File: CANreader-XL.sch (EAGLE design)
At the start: 100 parts, among them IC1 STM32F107RBT, IC2 TJA1055T/3, IC3 BD9G101G, IC4 LM1117IMPX-3.3, IC5 MCP2562-SOIC8, IC7 DP83848I, Q1 25MHz, SW1 SLEEP, SW2 TERM, U1 HC_05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

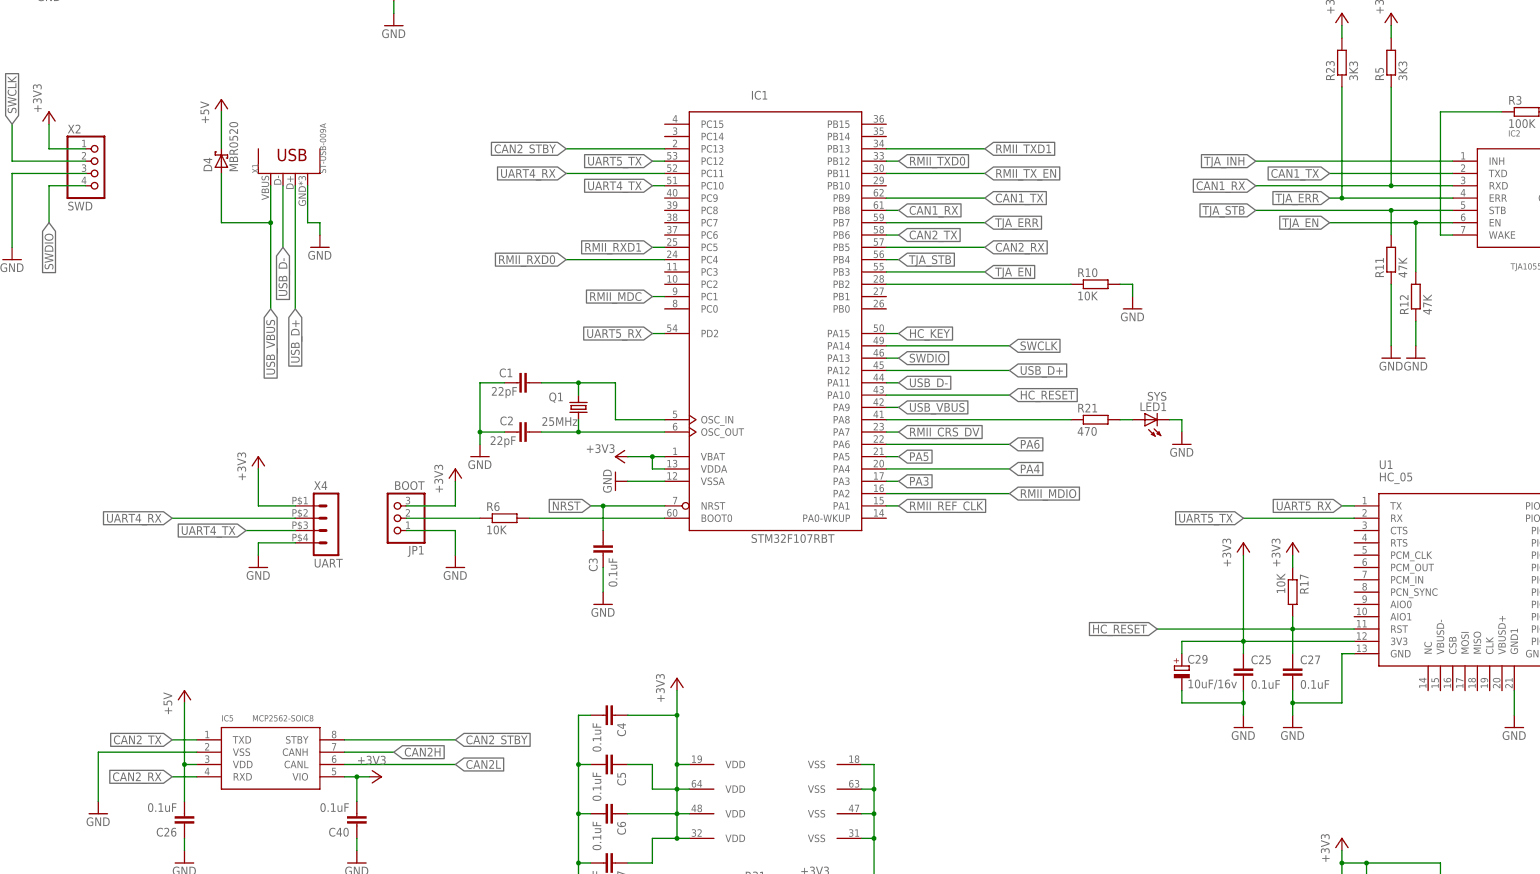
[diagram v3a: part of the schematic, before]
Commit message: Swap UART, CAN for better routing
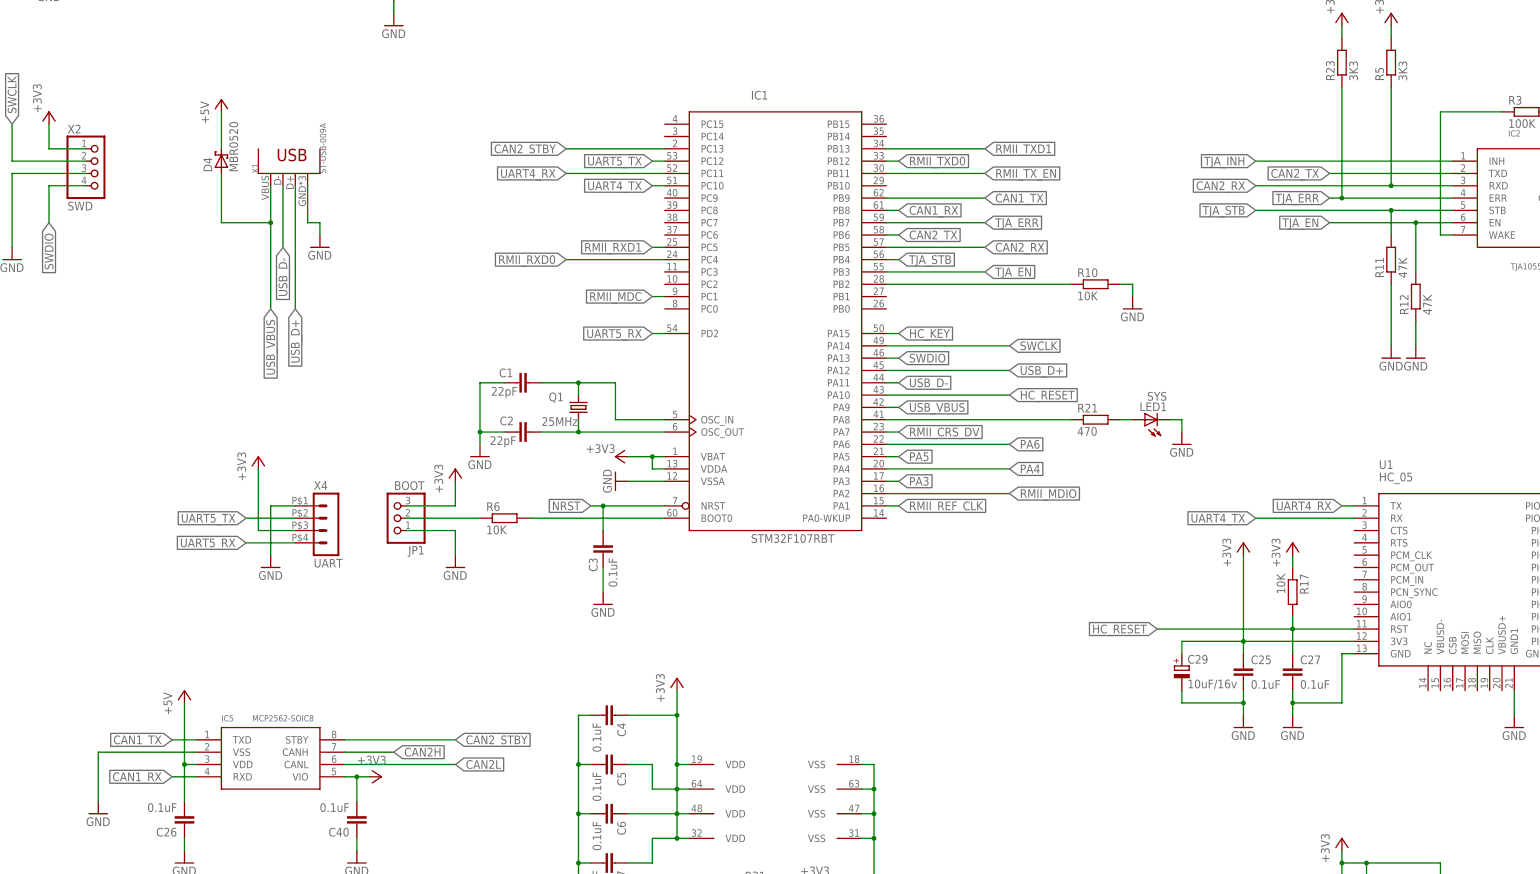
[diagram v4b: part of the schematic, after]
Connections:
- net +3V3: now also X4.3; no longer X4.1
- net CAN1_RX: now also IC5.RXD; no longer IC2.RXD, R5.1
- net CAN1_TX: now also IC5.TXD; no longer IC2.TXD
- net CAN2_RX: now also IC2.RXD, R5.1; no longer IC5.RXD
- net CAN2_TX: now also IC2.TXD; no longer IC5.TXD
- net GND: now also X4.1; no longer X4.4
- net UART4_RX: now also U1.TX; no longer X4.2
- net UART4_TX: now also U1.RX; no longer X4.3
- net UART5_RX: now also X4.4; no longer U1.TX
- net UART5_TX: now also X4.2; no longer U1.RX
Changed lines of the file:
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@@
 <?xml version="1.0" encoding="utf-8"?>
 <!DOCTYPE eagle SYSTEM "eagle.dtd">
-<eagle version="7.5.0">
+<eagle version="7.6.0">
 <drawing>
 <settings>
@@
 <instance part="R10" gate="G$1" x="139.7" y="45.72"/>
 <instance part="GND16" gate="1" x="7.62" y="-12.7"/>
-<instance part="GND17" gate="1" x="-33.02" y="-12.7"/>
+<instance part="GND17" gate="1" x="-30.48" y="-12.7"/>
 <instance part="D4" gate="D$1" x="-40.64" y="71.12" rot="R90"/>
 <instance part="GND18" gate="1" x="180.34" y="162.56" rot="R270"/>
@@
 <segment>
 <pinref part="GND17" gate="1" pin="GND"/>
-<wire x1="-25.4" y1="-7.62" x2="-33.02" y2="-7.62" width="0.1524" layer="91"/>
-<wire x1="-33.02" y1="-7.62" x2="-33.02" y2="-10.16" width="0.1524" layer="91"/>
-<pinref part="X4" gate="G$1" pin="4"/>
+<wire x1="-30.48" y1="-10.16" x2="-30.48" y2="0" width="0.1524" layer="91"/>
+<pinref part="X4" gate="G$1" pin="1"/>
+<wire x1="-30.48" y1="0" x2="-25.4" y2="0" width="0.1524" layer="91"/>
 </segment>
 <segment>
@@
 <segment>
 <pinref part="+3V9" gate="G$1" pin="+3V3"/>
-<wire x1="-25.4" y1="0" x2="-33.02" y2="0" width="0.1524" layer="91"/>
-<wire x1="-33.02" y1="0" x2="-33.02" y2="7.62" width="0.1524" layer="91"/>
-<pinref part="X4" gate="G$1" pin="1"/>
+<wire x1="-33.02" y1="-5.08" x2="-33.02" y2="7.62" width="0.1524" layer="91"/>
+<pinref part="X4" gate="G$1" pin="3"/>
+<wire x1="-33.02" y1="-5.08" x2="-25.4" y2="-5.08" width="0.1524" layer="91"/>
 </segment>
 <segment>
@@
 <net name="CAN1_RX" class="0">
 <segment>
-<pinref part="IC2" gate="G$1" pin="RXD"/>
-<pinref part="R5" gate="G$1" pin="1"/>
-<wire x1="200.66" y1="66.04" x2="213.36" y2="66.04" width="0.1524" layer="91"/>
-<wire x1="200.66" y1="86.36" x2="200.66" y2="66.04" width="0.1524" layer="91"/>
-<junction x="200.66" y="66.04"/>
-<wire x1="200.66" y1="66.04" x2="172.72" y2="66.04" width="0.1524" layer="91"/>
-<label x="172.72" y="66.04" size="1.778" layer="95" rot="R180" xref="yes"/>
-</segment>
-<segment>
 <label x="99.06" y="60.96" size="1.778" layer="95" xref="yes"/>
 <pinref part="IC1" gate="MCU" pin="PB8"/>
 <wire x1="99.06" y1="60.96" x2="96.52" y2="60.96" width="0.1524" layer="91"/>
+</segment>
+<segment>
+<pinref part="IC5" gate="G$1" pin="RXD"/>
+<wire x1="-45.72" y1="-55.88" x2="-50.8" y2="-55.88" width="0.1524" layer="91"/>
+<label x="-50.8" y="-55.88" size="1.778" layer="95" rot="R180" xref="yes"/>
 </segment>
 </net>
@@
 </segment>
 <segment>
-<label x="-50.8" y="-2.54" size="1.778" layer="95" rot="R180" xref="yes"/>
-<wire x1="-25.4" y1="-2.54" x2="-50.8" y2="-2.54" width="0.1524" layer="91"/>
-<pinref part="X4" gate="G$1" pin="2"/>
+<pinref part="U1" gate="G$1" pin="TX"/>
+<wire x1="193.04" y1="0" x2="190.5" y2="0" width="0.1524" layer="91"/>
+<label x="190.5" y="0" size="1.778" layer="95" rot="R180" xref="yes"/>
 </segment>
 </net>
@@
 </segment>
 <segment>
-<label x="-35.56" y="-5.08" size="1.778" layer="95" rot="R180" xref="yes"/>
-<wire x1="-35.56" y1="-5.08" x2="-25.4" y2="-5.08" width="0.1524" layer="91"/>
-<pinref part="X4" gate="G$1" pin="3"/>
+<pinref part="U1" gate="G$1" pin="RX"/>
+<wire x1="193.04" y1="-2.54" x2="172.72" y2="-2.54" width="0.1524" layer="91"/>
+<label x="172.72" y="-2.54" size="1.778" layer="95" rot="R180" xref="yes"/>
 </segment>
 </net>
@@
 </segment>
 <segment>
-<pinref part="U1" gate="G$1" pin="RX"/>
-<wire x1="193.04" y1="-2.54" x2="170.18" y2="-2.54" width="0.1524" layer="91"/>
-<label x="170.18" y="-2.54" size="1.778" layer="95" rot="R180" xref="yes"/>
+<pinref part="X4" gate="G$1" pin="2"/>
+<wire x1="-25.4" y1="-2.54" x2="-35.56" y2="-2.54" width="0.1524" layer="91"/>
+<label x="-35.56" y="-2.54" size="1.778" layer="95" rot="R180" xref="yes"/>
 </segment>
 </net>
@@
 </segment>
 <segment>
-<pinref part="U1" gate="G$1" pin="TX"/>
-<wire x1="193.04" y1="0" x2="190.5" y2="0" width="0.1524" layer="91"/>
-<label x="190.5" y="0" size="1.778" layer="95" rot="R180" xref="yes"/>
+<pinref part="X4" gate="G$1" pin="4"/>
+<wire x1="-25.4" y1="-7.62" x2="-35.56" y2="-7.62" width="0.1524" layer="91"/>
+<label x="-35.56" y="-7.62" size="1.778" layer="95" rot="R180" xref="yes"/>
 </segment>
 </net>
@@
 <net name="CAN1_TX" class="0">
 <segment>
-<pinref part="IC2" gate="G$1" pin="TXD"/>
-<wire x1="213.36" y1="68.58" x2="187.96" y2="68.58" width="0.1524" layer="91"/>
-<label x="187.96" y="68.58" size="1.778" layer="95" rot="R180" xref="yes"/>
-</segment>
-<segment>
 <label x="116.84" y="63.5" size="1.778" layer="95" xref="yes"/>
 <wire x1="96.52" y1="63.5" x2="116.84" y2="63.5" width="0.1524" layer="91"/>
 <pinref part="IC1" gate="MCU" pin="PB9"/>
+</segment>
+<segment>
+<pinref part="IC5" gate="G$1" pin="TXD"/>
+<wire x1="-45.72" y1="-48.26" x2="-50.8" y2="-48.26" width="0.1524" layer="91"/>
+<label x="-50.8" y="-48.26" size="1.778" layer="95" rot="R180" xref="yes"/>
 </segment>
 </net>
@@
 <net name="CAN2_TX" class="0">
 <segment>
-<wire x1="-45.72" y1="-48.26" x2="-50.8" y2="-48.26" width="0.1524" layer="91"/>
-<label x="-50.8" y="-48.26" size="1.778" layer="95" rot="R180" xref="yes"/>
-<pinref part="IC5" gate="G$1" pin="TXD"/>
-</segment>
-<segment>
 <label x="99.06" y="55.88" size="1.778" layer="95" xref="yes"/>
 <pinref part="IC1" gate="MCU" pin="PB6"/>
 <wire x1="99.06" y1="55.88" x2="96.52" y2="55.88" width="0.1524" layer="91"/>
 </segment>
+<segment>
+<pinref part="IC2" gate="G$1" pin="TXD"/>
+<wire x1="213.36" y1="68.58" x2="187.96" y2="68.58" width="0.1524" layer="91"/>
+<label x="187.96" y="68.58" size="1.778" layer="95" rot="R180" xref="yes"/>
+</segment>
 </net>
 <net name="CAN2_RX" class="0">
-<segment>
-<wire x1="-45.72" y1="-55.88" x2="-50.8" y2="-55.88" width="0.1524" layer="91"/>
-<label x="-50.8" y="-55.88" size="1.778" layer="95" rot="R180" xref="yes"/>
-<pinref part="IC5" gate="G$1" pin="RXD"/>
-</segment>
 <segment>
 <label x="116.84" y="53.34" size="1.778" layer="95" xref="yes"/>
@@
 <wire x1="116.84" y1="53.34" x2="96.52" y2="53.34" width="0.1524" layer="91"/>
 </segment>
-</net>
+<segment>
+<pinref part="IC2" gate="G$1" pin="RXD"/>
+<pinref part="R5" gate="G$1" pin="1"/>
+<wire x1="213.36" y1="66.04" x2="200.66" y2="66.04" width="0.1524" layer="91"/>
+<wire x1="200.66" y1="66.04" x2="200.66" y2="86.36" width="0.1524" layer="91"/>
+<wire x1="200.66" y1="66.04" x2="172.72" y2="66.04" width="0.1524" layer="91"/>
+<junction x="200.66" y="66.04"/>
+<label x="172.72" y="66.04" size="1.778" layer="95" rot="R180" xref="yes"/>
+</segment>
+</net>

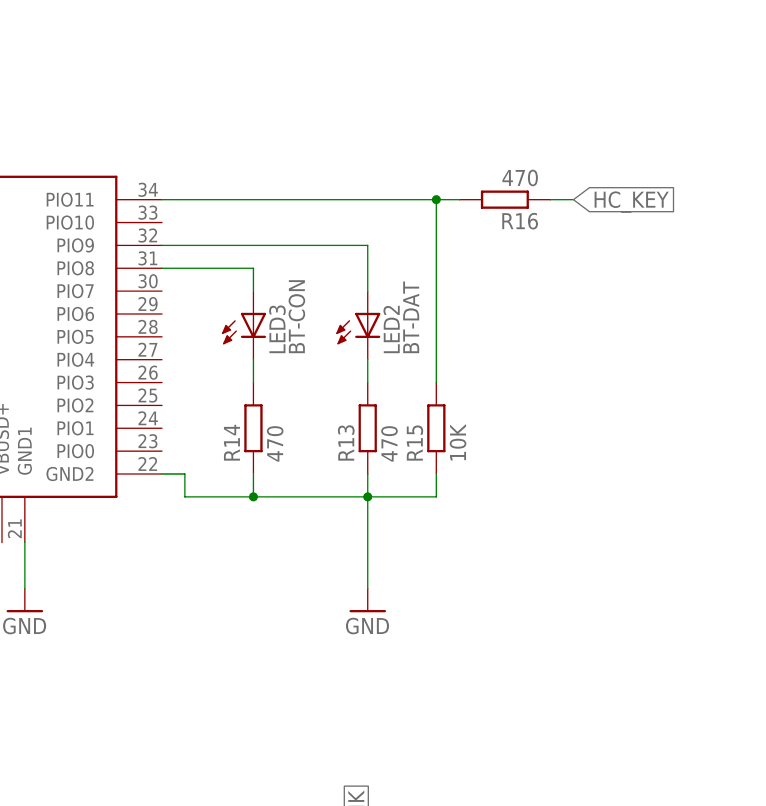
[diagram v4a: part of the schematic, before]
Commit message: Swap ports
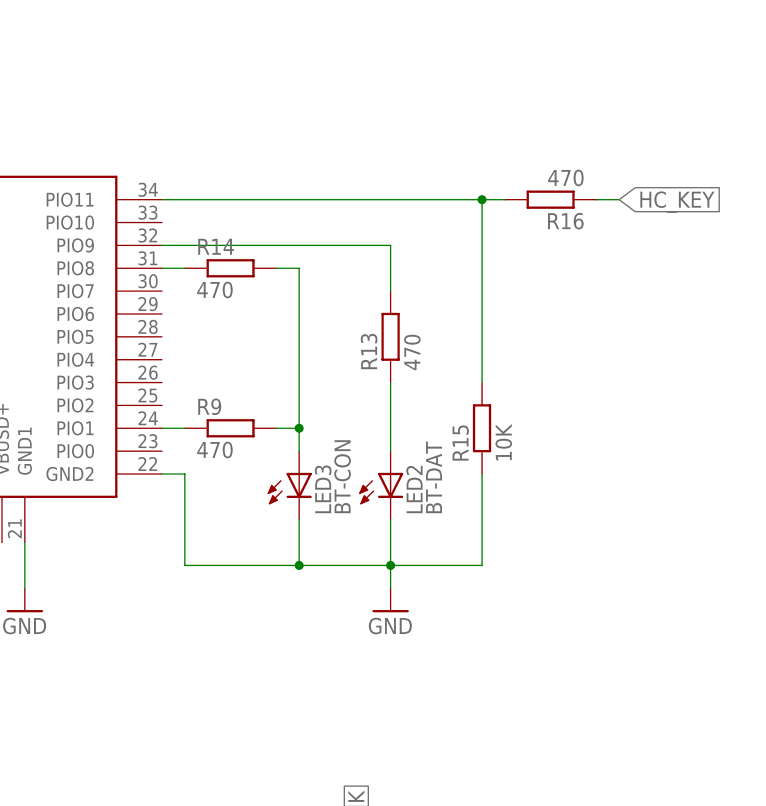
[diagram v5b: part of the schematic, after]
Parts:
- added R9: 470, rcl:R-EU_R0805
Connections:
- new net N$33: LED3.A, R14.2, R9.2
- net GND: now also LED2.C, LED3.C; no longer R13.1, R14.1
- net N$10: now also R13.2; no longer LED2.A
- net N$11: now also LED2.A, R13.1; no longer LED2.C, R13.2
- net N$13: now also R9.1, U1.PIO1; no longer LED3.C, R14.2
- net N$5: now also R14.1; no longer LED3.A
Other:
- moved on the sheet: LED2, LED3, R13, R14, R15, R16
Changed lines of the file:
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@@
 <part name="+3V7" library="supply1" deviceset="+3V3" device=""/>
 <part name="R6" library="rcl" deviceset="R-EU_" device="R0805" value="10K"/>
+<part name="R9" library="rcl" deviceset="R-EU_" device="R0805" value="470"/>
 </parts>
 <sheets>
@@
 <instance part="C25" gate="G$1" x="170.18" y="-33.02"/>
 <instance part="+3V5" gate="G$1" x="180.34" y="-7.62"/>
-<instance part="R13" gate="G$1" x="264.16" y="-25.4" rot="R90"/>
-<instance part="R14" gate="G$1" x="251.46" y="-25.4" rot="R90"/>
-<instance part="R15" gate="G$1" x="271.78" y="-25.4" rot="R90"/>
-<instance part="R16" gate="G$1" x="279.4" y="0" rot="R180"/>
+<instance part="R13" gate="G$1" x="266.7" y="-15.24" rot="R90"/>
+<instance part="R14" gate="G$1" x="248.92" y="-7.62"/>
+<instance part="R15" gate="G$1" x="276.86" y="-25.4" rot="R90"/>
+<instance part="R16" gate="G$1" x="284.48" y="0" rot="R180"/>
 <instance part="R17" gate="G$1" x="180.34" y="-17.78" rot="R270"/>
 <instance part="GND22" gate="1" x="12.7" y="10.16"/>
@@
 <instance part="GND31" gate="1" x="93.98" y="-83.82"/>
 <instance part="R22" gate="G$1" x="-43.18" y="-106.68" rot="R270"/>
-<instance part="LED2" gate="G$1" x="264.16" y="-12.7"/>
-<instance part="LED3" gate="G$1" x="251.46" y="-12.7"/>
+<instance part="LED2" gate="G$1" x="266.7" y="-30.48"/>
+<instance part="LED3" gate="G$1" x="256.54" y="-30.48"/>
 <instance part="LED1" gate="G$1" x="149.86" y="17.78" rot="R90"/>
 <instance part="SW2" gate="G$1" x="-55.88" y="-104.14"/>
@@
 <instance part="C27" gate="G$1" x="180.34" y="-33.02"/>
 <instance part="GND33" gate="1" x="180.34" y="-45.72"/>
-<instance part="GND34" gate="1" x="264.16" y="-45.72"/>
+<instance part="GND34" gate="1" x="266.7" y="-45.72"/>
 <instance part="GND35" gate="1" x="170.18" y="-45.72"/>
 <instance part="C11" gate="G$1" x="106.68" y="132.08"/>
@@
 <instance part="+3V7" gate="G$1" x="7.62" y="7.62"/>
 <instance part="R6" gate="G$1" x="17.78" y="-2.54"/>
+<instance part="R9" gate="G$1" x="248.92" y="-25.4"/>
 </instances>
 <busses>
@@
 <pinref part="U1" gate="G$1" pin="GND2"/>
 <wire x1="243.84" y1="-30.48" x2="241.3" y2="-30.48" width="0.1524" layer="91"/>
-<wire x1="243.84" y1="-33.02" x2="243.84" y2="-30.48" width="0.1524" layer="91"/>
+<wire x1="243.84" y1="-40.64" x2="243.84" y2="-30.48" width="0.1524" layer="91"/>
 <pinref part="R15" gate="G$1" pin="1"/>
-<wire x1="264.16" y1="-33.02" x2="251.46" y2="-33.02" width="0.1524" layer="91"/>
-<wire x1="251.46" y1="-33.02" x2="243.84" y2="-33.02" width="0.1524" layer="91"/>
-<wire x1="271.78" y1="-30.48" x2="271.78" y2="-33.02" width="0.1524" layer="91"/>
-<wire x1="271.78" y1="-33.02" x2="264.16" y2="-33.02" width="0.1524" layer="91"/>
-<pinref part="R13" gate="G$1" pin="1"/>
-<wire x1="264.16" y1="-30.48" x2="264.16" y2="-33.02" width="0.1524" layer="91"/>
-<junction x="264.16" y="-33.02"/>
-<pinref part="R14" gate="G$1" pin="1"/>
-<wire x1="251.46" y1="-30.48" x2="251.46" y2="-33.02" width="0.1524" layer="91"/>
-<junction x="251.46" y="-33.02"/>
+<wire x1="266.7" y1="-40.64" x2="256.54" y2="-40.64" width="0.1524" layer="91"/>
+<wire x1="256.54" y1="-40.64" x2="243.84" y2="-40.64" width="0.1524" layer="91"/>
+<wire x1="276.86" y1="-30.48" x2="276.86" y2="-40.64" width="0.1524" layer="91"/>
+<wire x1="276.86" y1="-40.64" x2="266.7" y2="-40.64" width="0.1524" layer="91"/>
+<junction x="266.7" y="-40.64"/>
 <pinref part="GND34" gate="1" pin="GND"/>
-<wire x1="264.16" y1="-33.02" x2="264.16" y2="-43.18" width="0.1524" layer="91"/>
+<wire x1="266.7" y1="-40.64" x2="266.7" y2="-43.18" width="0.1524" layer="91"/>
+<pinref part="LED3" gate="G$1" pin="C"/>
+<wire x1="256.54" y1="-35.56" x2="256.54" y2="-40.64" width="0.1524" layer="91"/>
+<junction x="256.54" y="-40.64"/>
+<pinref part="LED2" gate="G$1" pin="C"/>
+<wire x1="266.7" y1="-35.56" x2="266.7" y2="-40.64" width="0.1524" layer="91"/>
 </segment>
 <segment>
@@
 <pinref part="U1" gate="G$1" pin="PIO11"/>
 <pinref part="R15" gate="G$1" pin="2"/>
-<wire x1="241.3" y1="0" x2="271.78" y2="0" width="0.1524" layer="91"/>
-<wire x1="271.78" y1="0" x2="271.78" y2="-20.32" width="0.1524" layer="91"/>
+<wire x1="241.3" y1="0" x2="276.86" y2="0" width="0.1524" layer="91"/>
+<wire x1="276.86" y1="0" x2="276.86" y2="-20.32" width="0.1524" layer="91"/>
 <pinref part="R16" gate="G$1" pin="2"/>
-<wire x1="271.78" y1="0" x2="274.32" y2="0" width="0.1524" layer="91"/>
-<junction x="271.78" y="0"/>
+<wire x1="276.86" y1="0" x2="279.4" y2="0" width="0.1524" layer="91"/>
+<junction x="276.86" y="0"/>
 </segment>
 </net>
@@
 <segment>
 <pinref part="R16" gate="G$1" pin="1"/>
-<wire x1="284.48" y1="0" x2="287.02" y2="0" width="0.1524" layer="91"/>
-<label x="287.02" y="0" size="1.778" layer="95" xref="yes"/>
+<wire x1="289.56" y1="0" x2="292.1" y2="0" width="0.1524" layer="91"/>
+<label x="292.1" y="0" size="1.778" layer="95" xref="yes"/>
 </segment>
 <segment>
@@
 </segment>
 </net>
-<net name="N$11" class="0">
-<segment>
-<pinref part="LED2" gate="G$1" pin="C"/>
-<pinref part="R13" gate="G$1" pin="2"/>
-<wire x1="264.16" y1="-17.78" x2="264.16" y2="-20.32" width="0.1524" layer="91"/>
-</segment>
-</net>
-<net name="N$13" class="0">
-<segment>
-<pinref part="LED3" gate="G$1" pin="C"/>
-<pinref part="R14" gate="G$1" pin="2"/>
-<wire x1="251.46" y1="-17.78" x2="251.46" y2="-20.32" width="0.1524" layer="91"/>
-</segment>
-</net>
 <net name="N$4" class="0">
 <segment>
@@
 <net name="N$5" class="0">
 <segment>
-<pinref part="LED3" gate="G$1" pin="A"/>
-<wire x1="251.46" y1="-10.16" x2="251.46" y2="-7.62" width="0.1524" layer="91"/>
 <pinref part="U1" gate="G$1" pin="PIO8"/>
-<wire x1="251.46" y1="-7.62" x2="241.3" y2="-7.62" width="0.1524" layer="91"/>
+<wire x1="243.84" y1="-7.62" x2="241.3" y2="-7.62" width="0.1524" layer="91"/>
+<pinref part="R14" gate="G$1" pin="1"/>
 </segment>
 </net>
@@
 <segment>
 <pinref part="U1" gate="G$1" pin="PIO9"/>
-<wire x1="241.3" y1="-5.08" x2="264.16" y2="-5.08" width="0.1524" layer="91"/>
-<pinref part="LED2" gate="G$1" pin="A"/>
-<wire x1="264.16" y1="-5.08" x2="264.16" y2="-10.16" width="0.1524" layer="91"/>
+<wire x1="241.3" y1="-5.08" x2="266.7" y2="-5.08" width="0.1524" layer="91"/>
+<pinref part="R13" gate="G$1" pin="2"/>
+<wire x1="266.7" y1="-5.08" x2="266.7" y2="-10.16" width="0.1524" layer="91"/>
 </segment>
 </net>
@@
 </segment>
 </net>
+<net name="N$13" class="0">
+<segment>
+<pinref part="U1" gate="G$1" pin="PIO1"/>
+<pinref part="R9" gate="G$1" pin="1"/>
+<wire x1="241.3" y1="-25.4" x2="243.84" y2="-25.4" width="0.1524" layer="91"/>
+</segment>
+</net>
+<net name="N$33" class="0">
+<segment>
+<pinref part="R9" gate="G$1" pin="2"/>
+<pinref part="LED3" gate="G$1" pin="A"/>
+<wire x1="254" y1="-25.4" x2="256.54" y2="-25.4" width="0.1524" layer="91"/>
+<wire x1="256.54" y1="-25.4" x2="256.54" y2="-27.94" width="0.1524" layer="91"/>
+<pinref part="R14" gate="G$1" pin="2"/>
+<wire x1="254" y1="-7.62" x2="256.54" y2="-7.62" width="0.1524" layer="91"/>
+<wire x1="256.54" y1="-7.62" x2="256.54" y2="-25.4" width="0.1524" layer="91"/>
+<junction x="256.54" y="-25.4"/>
+</segment>
+</net>
+<net name="N$11" class="0">
+<segment>
+<pinref part="R13" gate="G$1" pin="1"/>
+<pinref part="LED2" gate="G$1" pin="A"/>
+<wire x1="266.7" y1="-20.32" x2="266.7" y2="-27.94" width="0.1524" layer="91"/>
+</segment>
+</net>
